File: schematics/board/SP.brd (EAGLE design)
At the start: 82 x 82 mm, 45 parts

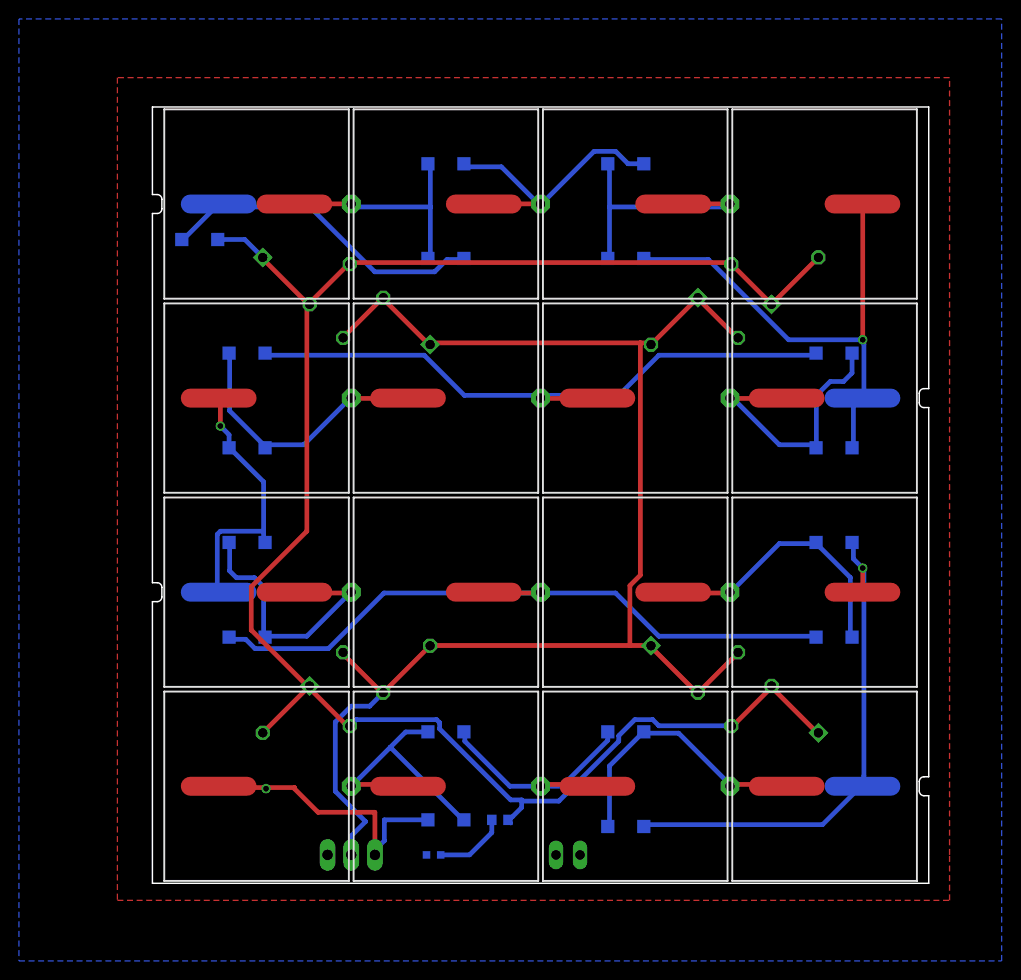
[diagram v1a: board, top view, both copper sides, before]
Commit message: SP, убраны диоды, изменены площадки, добавлены надписи
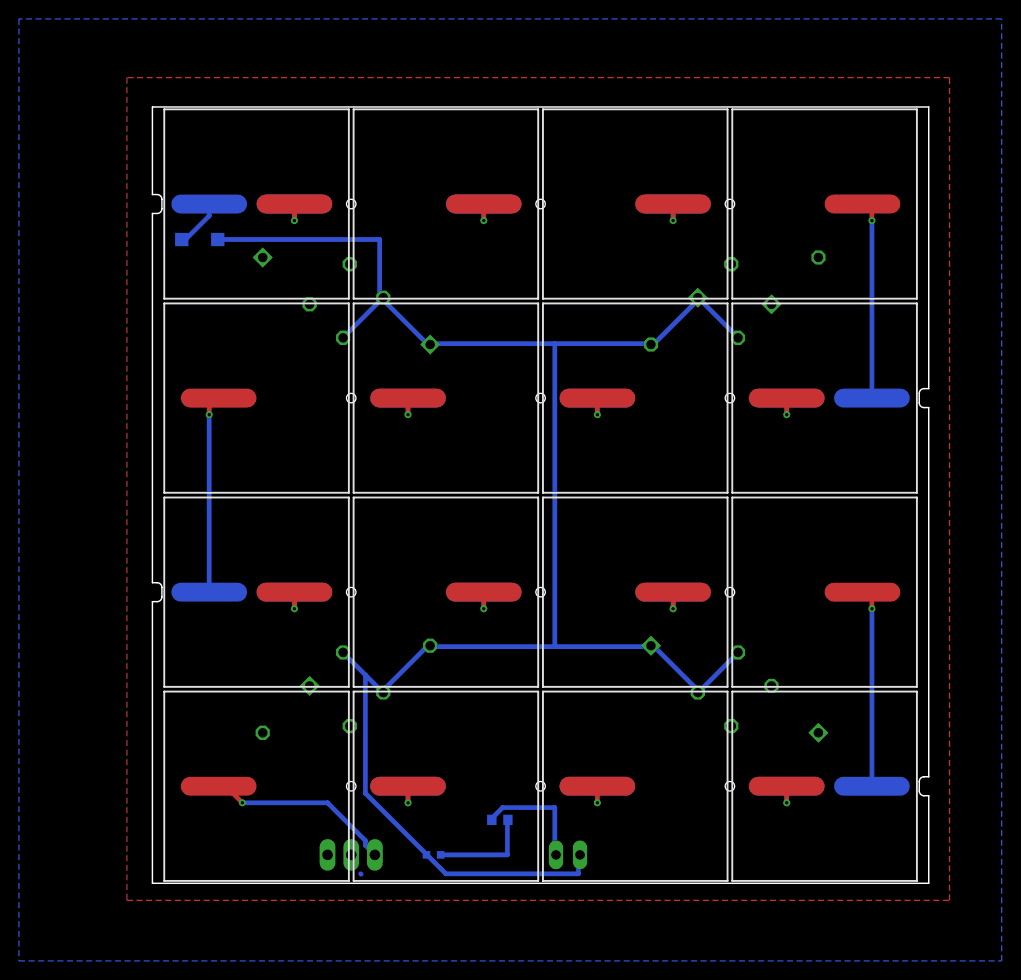
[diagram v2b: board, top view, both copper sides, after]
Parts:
- removed D23, D24, D25, D26, D27, D28, D29, D30, D31, D32, D33, D34, D35, D36, D37, D38: MBR0520LT, diode:SOD123
- renumbered R1 to R1_2K7
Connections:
- removed net BUS+1: D1.C, JP1.1, R1_2K7.2, U$1.1, U$1.2, U$1.4, U$18.1, U$18.2, U$18.3, U$20.1, U$20.2, U$20.4, U$3.1, U$3.2, U$3.3
- removed net BUS-1: D29.A, S1.3, SOL1.IN
- removed net N$19: D25.C, D26.A, SOL4.OUT, SOL5.IN
- removed net N$2: JP1.2, PWR.C, S1.2, U$19.2, U$19.3, U$19.4, U$2.1, U$2.2, U$2.4, U$21.1, U$21.2, U$21.4, U$4.1, U$4.2, U$4.3
- removed net N$22: D26.C, D27.A, SOL5.OUT, SOL6.IN
- removed net N$28: D28.C, D30.A, SOL7.OUT, SOL8.IN
- new net BUS+: JP1.2, R1_2K7.1, S1.2, U$1.1, U$1.2, U$1.4, U$18.1, U$18.2, U$18.3, U$20.1, U$20.2, U$20.4, U$3.1, U$3.2, U$3.3
- new net BUS-: D1.C, JP1.1, PWR.C, U$19.2, U$19.3, U$19.4, U$2.1, U$2.2, U$2.4, U$21.1, U$21.2, U$21.4, U$4.1, U$4.2, U$4.3
- new net N$17: SOL14.OUT, SOL15.IN
- new net N$18: SOL15.OUT, SOL16.IN
- new net N$24: SOL4.OUT, SOL5.IN
- new net N$7: S1.3, SOL1.IN
- net N$1: no longer D23.A, D29.C
- net N$10: now also SOL7.OUT, SOL8.IN; no longer D32.C, D33.A, SOL10.OUT, SOL11.IN
- net N$11: now also SOL8.OUT, SOL9.IN; no longer D33.C, D34.A, SOL11.OUT, SOL12.IN
- net N$12: now also SOL10.IN, SOL9.OUT; no longer D34.C, D35.A, SOL12.OUT, SOL13.IN
- net N$13: now also SOL10.OUT, SOL11.IN; no longer D35.C, D36.A, SOL13.OUT, SOL14.IN
- net N$14: now also SOL11.OUT, SOL12.IN; no longer D36.C, D37.A, SOL14.OUT, SOL15.IN
- net N$15: now also SOL12.OUT, SOL13.IN; no longer D37.C, D38.A, SOL15.OUT, SOL16.IN
- net N$16: now also SOL13.OUT, SOL14.IN; no longer D23.C, D24.A, SOL2.OUT, SOL3.IN
- net N$3: now also SOL2.OUT, SOL3.IN; no longer D24.C, D25.A, SOL3.OUT, SOL4.IN
- net N$4: no longer D38.C
- net N$5: now also R1_2K7.2; no longer R1_2K7.1
- net N$6: now also SOL3.OUT, SOL4.IN; no longer D27.C, D28.A, SOL6.OUT, SOL7.IN
- net N$8: now also SOL5.OUT, SOL6.IN; no longer D30.C, D31.A, SOL8.OUT, SOL9.IN
- net N$9: now also SOL6.OUT, SOL7.IN; no longer D31.C, D32.A, SOL10.IN, SOL9.OUT
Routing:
- net BUS+1: track 195.8 -> 0.00 mm
- net BUS-: track 0.00 -> 195.4 mm
- net N$2: track 153.8 -> 0.00 mm
- net N$6: track 73.0 -> 3.50 mm, vias 0 -> 1
- net N$10: track 68.3 -> 3.50 mm, vias 0 -> 1
- net N$19: track 53.6 -> 0.00 mm, vias 1 -> 0
- net N$12: track 53.1 -> 3.50 mm
- net BUS-1: track 31.0 -> 0.00 mm, vias 1 -> 0
- net N$28: track 29.9 -> 0.00 mm
- net N$4: track 34.9 -> 5.19 mm
- net N$22: track 28.9 -> 0.06 mm
- net N$14: track 29.7 -> 3.50 mm, vias 0 -> 1
- net N$3: track 29.3 -> 3.50 mm, vias 0 -> 1
- net N$13: track 29.2 -> 3.50 mm, vias 0 -> 1
- net N$9: track 28.9 -> 3.50 mm, vias 0 -> 1
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- added copper zone on layer 1, net BUS+
- added copper zone on layer 16, net N$22
- removed copper zone on layer 1, net BUS+1
- removed copper zone on layer 16, net N$2
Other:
- board text added: "OFF"
- board text added: "ON"

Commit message: Созданы новые gerber файлы плат SP и BSK2 версии 1.1
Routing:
- net BUS-: track 195.4 -> 191.0 mm
- net N$4: track 5.19 -> 6.65 mm
- added copper zone on layer 16, net BUS-
- removed copper zone on layer 16, net N$22
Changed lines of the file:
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@@
 <?xml version="1.0" encoding="utf-8"?>
 <!DOCTYPE eagle SYSTEM "eagle.dtd">
-<eagle version="9.5.2">
+<eagle version="9.4.2">
 <drawing>
 <settings>
-<setting alwaysvectorfont="no"/>
+<setting alwaysvectorfont="yes"/>
 <setting verticaltext="up"/>
 </settings>
@@
 <wire x1="42.5" y1="3" x2="42.63" y2="3" width="0.5" layer="16"/>
 </signal>
-<signal name="N$22">
-<polygon width="0.5" layer="16" isolate="0.5">
-<vertex x="-14.1" y="-8.2"/>
-<vertex x="89.7" y="-8.2"/>
-<vertex x="89.7" y="91.3"/>
-<vertex x="-14.1" y="91.3"/>
-</polygon>
-<wire x1="22" y1="1" x2="22.042125" y2="0.957875" width="0.5" layer="16"/>
-</signal>
 <signal name="N$7">
 <contactref element="SOL1" pad="IN"/>
@@
 <wire x1="52.5" y1="57" x2="52.66380625" y2="56.90644375" width="0.5" layer="16"/>
 <wire x1="29.5" y1="57" x2="29.336196875" y2="56.90644375" width="0.5" layer="16"/>
-<wire x1="31" y1="1" x2="29" y2="3" width="0.5" layer="16"/>
-<wire x1="45" y1="1" x2="31" y2="1" width="0.5" layer="16"/>
-<wire x1="45" y1="3" x2="45" y2="1" width="0.5" layer="16"/>
+<wire x1="45" y1="1" x2="45" y2="3" width="0.5" layer="16"/>
 <wire x1="45" y1="3" x2="45.17" y2="3" width="0.5" layer="16"/>
 <wire x1="24" y1="20.5" x2="22.5" y2="22" width="0.5" layer="16"/>
@@
 <wire x1="29.5" y1="25" x2="29.336196875" y2="25.093553125" width="0.5" layer="16"/>
 <wire x1="52.5" y1="25" x2="52.66380625" y2="25.093553125" width="0.5" layer="16"/>
-<wire x1="22.5" y1="9.5" x2="29" y2="3" width="0.5" layer="16"/>
+<wire x1="22.5" y1="9.5" x2="26.5" y2="5.5" width="0.5" layer="16"/>
 <wire x1="22.5" y1="22" x2="22.5" y2="9.5" width="0.5" layer="16"/>
-<wire x1="29" y1="3" x2="28.95" y2="3" width="0.5" layer="16"/>
 <wire x1="42.5" y1="25" x2="42.5" y2="57" width="0.5" layer="16"/>
+<polygon width="0.5" layer="16" isolate="0.5">
+<vertex x="-14.1" y="-8.2"/>
+<vertex x="89.7" y="-8.2"/>
+<vertex x="89.7" y="91.3"/>
+<vertex x="-14.1" y="91.3"/>
+</polygon>
+<wire x1="28.95" y1="1" x2="45" y2="1" width="0.5" layer="16"/>
 </signal>
 <signal name="N$4">
 <contactref element="SOL16" pad="OUT"/>
 <contactref element="D1" pad="A"/>
-<wire x1="6" y1="70.5" x2="3.5" y2="68" width="0.5" layer="16"/>
-<wire x1="6" y1="71.75" x2="6" y2="70.5" width="0.5" layer="16"/>
-<wire x1="3.5" y1="68" x2="3.1" y2="68" width="0.5" layer="16"/>
+<wire x1="3.1" y1="68" x2="3.1" y2="71.75" width="0.5" layer="16"/>
+<wire x1="3.1" y1="71.75" x2="6" y2="71.75" width="0.5" layer="16"/>
 </signal>
 <signal name="N$5">

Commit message: Подготовлены к производству платы ARK v1.1 и SP v 1.2
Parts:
- added D10, D11, D12, D13, D14, D15, D16, D17, D2, D3, D4, D5, D6, D7, D8, D9: MBR0520LT, diode:SOD123
- moved PWR 2.75 mm to (32.0, 1.50)
- moved R1_2K7 1.84 mm to (36.0, 5.00), turned to 0 degrees
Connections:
- net N$1: now also D16.A, D17.C
- net N$10: now also D10.A, D11.C
- net N$11: now also D10.C, D9.A
- net N$12: now also D8.A, D9.C
- net N$13: now also D7.A, D8.C
- net N$14: now also D6.A, D7.C
- net N$15: now also D5.A, D6.C
- net N$16: now also D4.A, D5.C
- net N$17: now also D3.A, D4.C
- net N$18: now also D2.A, D3.C
- net N$24: now also D13.A, D14.C
- net N$3: now also D15.A, D16.C
- net N$4: now also D2.C
- net N$6: now also D14.A, D15.C
- net N$7: now also D17.A
- net N$8: now also D12.A, D13.C
- net N$9: now also D11.A, D12.C
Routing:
- net BUS-: track 191.0 -> 76.0 mm
- net N$9: track 3.50 -> 64.6 mm
- net N$13: track 3.50 -> 58.2 mm
- net N$18: track 3.50 -> 32.5 mm
- net N$17: track 3.50 -> 32.5 mm
- net N$16: track 3.50 -> 32.5 mm
- net N$1: track 3.50 -> 31.3 mm
- net N$6: track 3.50 -> 29.0 mm
- net N$12: track 3.50 -> 29.0 mm
- net N$8: track 3.50 -> 28.0 mm
- net N$3: track 3.50 -> 25.1 mm
- net N$10: track 3.50 -> 22.0 mm
- net N$14: track 3.50 -> 18.5 mm
- net N$24: track 21.5 -> 35.8 mm
- net N$15: track 21.5 -> 35.8 mm
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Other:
- outline, holes or cut-outs redrawn
